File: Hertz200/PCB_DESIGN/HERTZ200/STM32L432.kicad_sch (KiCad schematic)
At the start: 10 parts

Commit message: schematics_Power_section
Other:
- moved on the sheet: C?
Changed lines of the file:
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@@
     (stroke (width 0) (type default) (color 0 0 0 0))
   )
-  (wire (pts (xy 96.52 71.12) (xy 96.52 73.66))
+  (wire (pts (xy 96.52 74.93) (xy 96.52 77.47))
     (stroke (width 0) (type default) (color 0 0 0 0))
   )
@@
     (stroke (width 0) (type default) (color 0 0 0 0))
   )
-  (wire (pts (xy 96.52 63.5) (xy 96.52 66.04))
+  (wire (pts (xy 96.52 63.5) (xy 96.52 69.85))
     (stroke (width 0) (type default) (color 0 0 0 0))
   )
@@
     (pin "1")
   )
-  (symbol (lib_id "power:GND") (at 96.52 73.66 0) (unit 1)
-    (in_bom yes) (on_board yes) (fields_autoplaced)
-    (property "Reference" "#PWR?" (id 0) (at 96.52 80.01 0)
-      (effects (font (size 1.27 1.27)) hide)
-    )
-    (property "Value" "GND" (id 1) (at 96.52 78.74 0))
-    (property "Footprint" "" (id 2) (at 96.52 73.66 0)
-      (effects (font (size 1.27 1.27)) hide)
-    )
-    (property "Datasheet" "" (id 3) (at 96.52 73.66 0)
+  (symbol (lib_id "power:GND") (at 96.52 77.47 0) (unit 1)
+    (in_bom yes) (on_board yes) (fields_autoplaced)
+    (property "Reference" "#PWR?" (id 0) (at 96.52 83.82 0)
+      (effects (font (size 1.27 1.27)) hide)
+    )
+    (property "Value" "GND" (id 1) (at 96.52 82.55 0))
+    (property "Footprint" "" (id 2) (at 96.52 77.47 0)
+      (effects (font (size 1.27 1.27)) hide)
+    )
+    (property "Datasheet" "" (id 3) (at 96.52 77.47 0)
       (effects (font (size 1.27 1.27)) hide)
     )
@@
     (pin "2")
   )
-  (symbol (lib_id "Device:C_Small") (at 96.52 68.58 0) (unit 1)
-    (in_bom yes) (on_board yes) (fields_autoplaced)
-    (property "Reference" "C?" (id 0) (at 99.06 67.3162 0)
-      (effects (font (size 1.27 1.27)) (justify left))
-    )
-    (property "Value" "0.1uF" (id 1) (at 99.06 69.8562 0)
-      (effects (font (size 1.27 1.27)) (justify left))
-    )
-    (property "Footprint" "" (id 2) (at 96.52 68.58 0)
-      (effects (font (size 1.27 1.27)) hide)
-    )
-    (property "Datasheet" "~" (id 3) (at 96.52 68.58 0)
-      (effects (font (size 1.27 1.27)) hide)
-    )
+  (symbol (lib_id "Device:C_Small") (at 96.52 72.39 0) (unit 1)
+    (in_bom yes) (on_board yes) (fields_autoplaced)
+    (property "Reference" "C?" (id 0) (at 99.06 71.1262 0)
+      (effects (font (size 1.27 1.27)) (justify left))
+    )
+    (property "Value" "0.1uF" (id 1) (at 99.06 73.6662 0)
+      (effects (font (size 1.27 1.27)) (justify left))
+    )
+    (property "Footprint" "" (id 2) (at 96.52 72.39 0)
+      (effects (font (size 1.27 1.27)) hide)
+    )
+    (property "Datasheet" "~" (id 3) (at 96.52 72.39 0)
+      (effects (font (size 1.27 1.27)) hide)
+    )

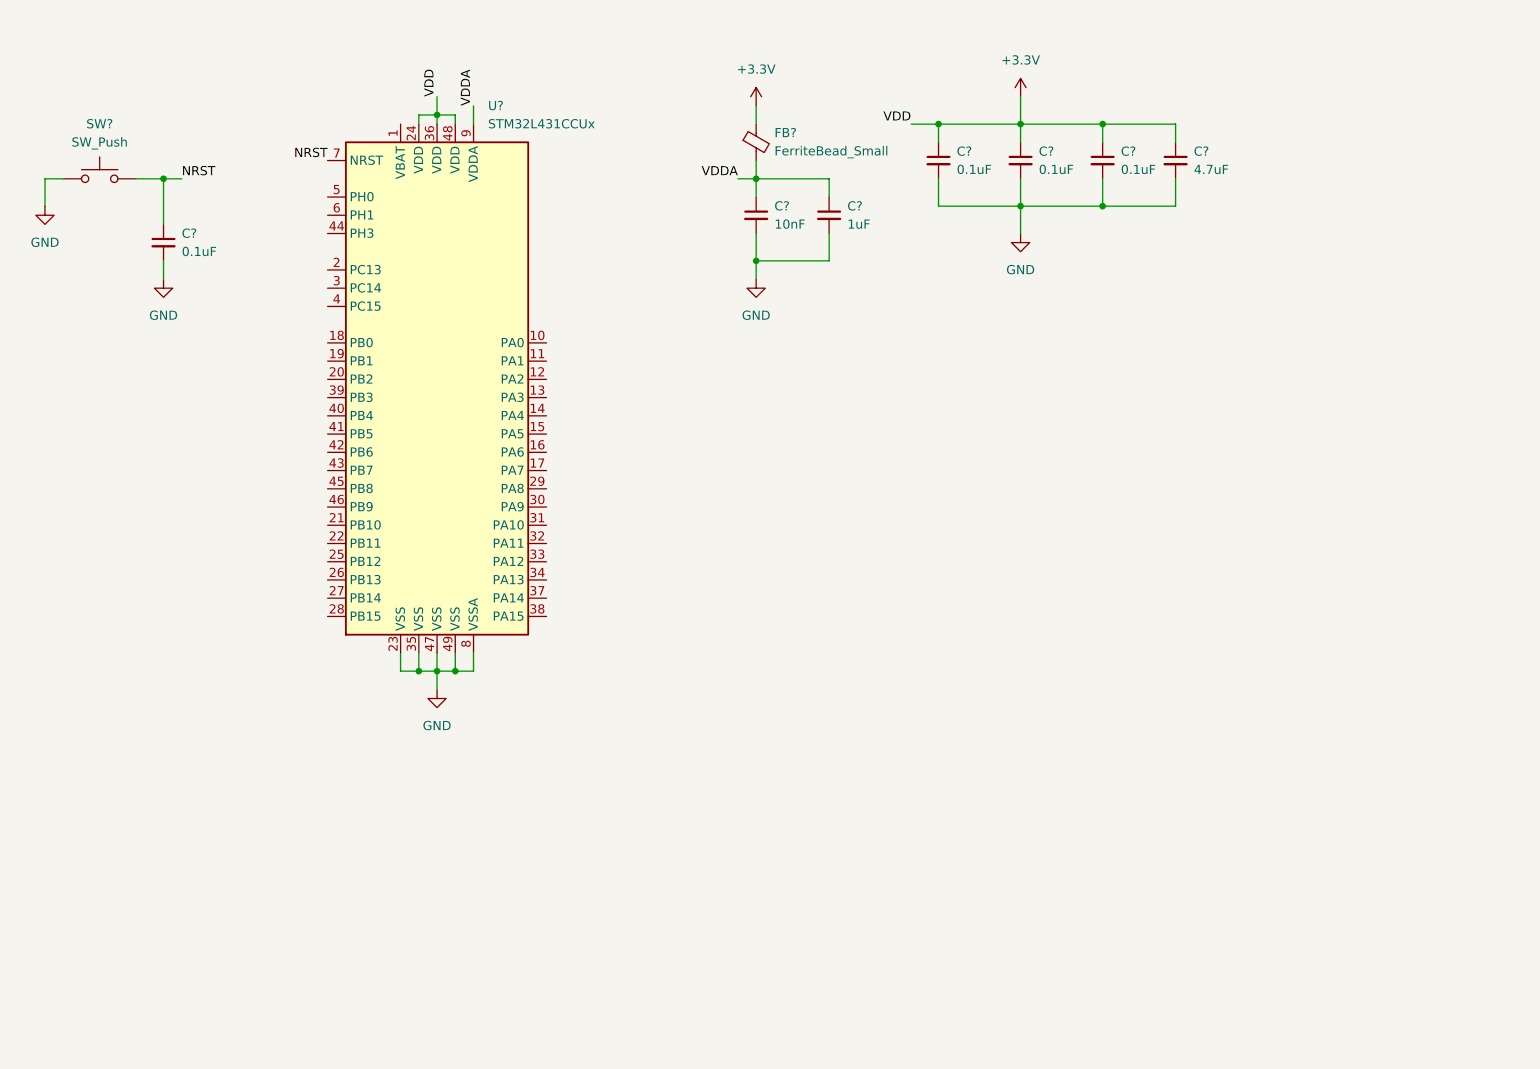
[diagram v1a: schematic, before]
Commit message: MCU-PIN-ASSIGNMENT
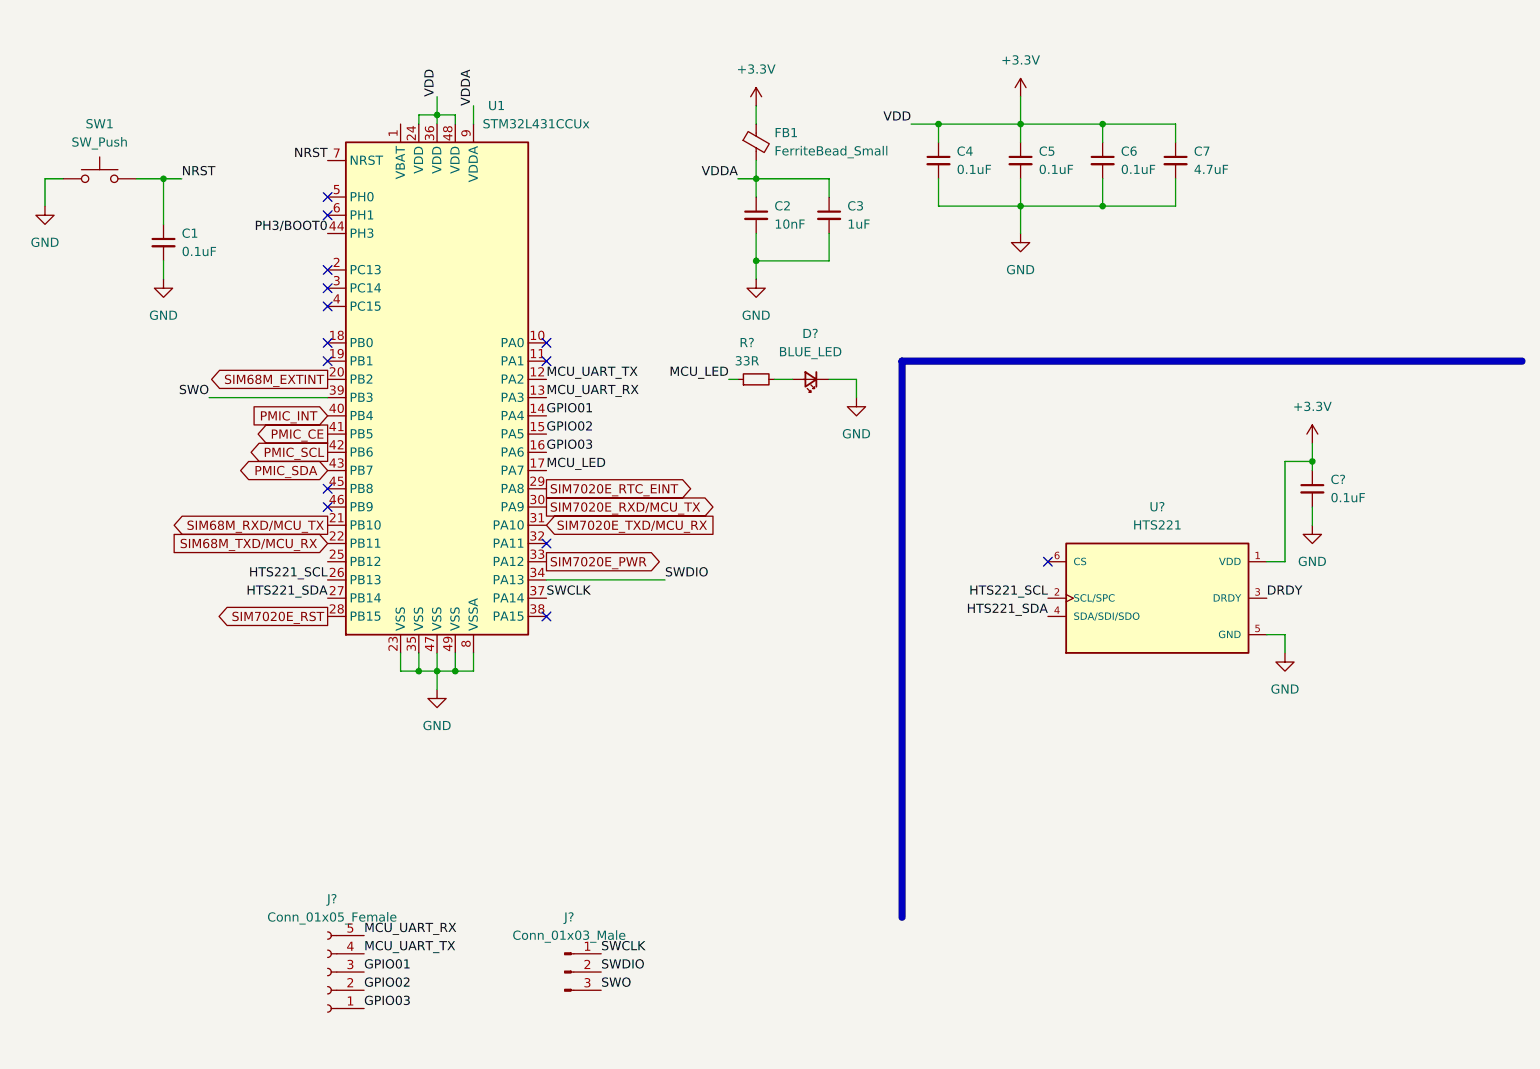
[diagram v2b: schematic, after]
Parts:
- added C?: 0.1uF, symbol Device:C_Small
- added D?: BLUE_LED, symbol Device:LED_Small
- added J?: Conn_01x03_Male, symbol Connector:Conn_01x03_Male
- added J?: Conn_01x05_Female, symbol Connector:Conn_01x05_Female
- added R?: 33R, symbol Device:R_Small
- added U?: HTS221, XDCR_HTS221, symbol HTS221:HTS221
- gave numbers to parts that had none: 10
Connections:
- net +3V3: now also C?.1, U?.1 (VDD)
- net GND: now also C?.2, D?.1 (K), U?.5 (GND)
- net MCU_UART_TX: now reaches U1.12 (PA2)
- net MCU_UART_TX: now also J?.4 (Pin_4)
- net MCU_UART_RX: now reaches U1.13 (PA3)
- net MCU_UART_RX: now also J?.5 (Pin_5)
- net GPIO01: now reaches U1.14 (PA4)
- net GPIO01: now also J?.3 (Pin_3)
- net GPIO02: now reaches U1.15 (PA5)
- net GPIO02: now also J?.2 (Pin_2)
- net GPIO03: now reaches U1.16 (PA6)
- net GPIO03: now also J?.1 (Pin_1)
- net MCU_LED: now reaches U1.17 (PA7)
- net MCU_LED: now also R?.1
- net SIM68M_EXTINT: now reaches U1.20 (PB2)
- net SIM68M_RXD/MCU_TX: now reaches U1.21 (PB10)
- net SIM68M_TXD/MCU_RX: now reaches U1.22 (PB11)
- net HTS221_SCL: now reaches U1.26 (PB13)
- net HTS221_SCL: now also U?.2 (SCL/SPC)
- net HTS221_SDA: now reaches U1.27 (PB14)
- net HTS221_SDA: now also U?.4 (SDA/SDI/SDO)
- net SIM7020E_RST: now reaches U1.28 (PB15)
- net SIM7020E_RTC_EINT: now reaches U1.29 (PA8)
- net SIM7020E_RXD/MCU_TX: now reaches U1.30 (PA9)
- net SIM7020E_TXD/MCU_RX: now reaches U1.31 (PA10)
- net SIM7020E_PWR: now reaches U1.33 (PA12)
- net SWDIO: now reaches U1.34 (PA13)
- net SWDIO: now also J?.2 (Pin_2)
- net SWCLK: now reaches U1.37 (PA14)
- net SWCLK: now also J?.1 (Pin_1)
- net SWO: now reaches U1.39 (PB3)
- net SWO: now also J?.3 (Pin_3)
- net PMIC_INT: now reaches U1.40 (PB4)
- net PMIC_CE: now reaches U1.41 (PB5)
- net PMIC_SCL: now reaches U1.42 (PB6)
- net PMIC_SDA: now reaches U1.43 (PB7)
- net PH3/BOOT0: now reaches U1.44 (PH3)
- new net: D?.2 (A), R?.2
- new net DRDY: U?.3 (DRDY)
- no-connect marks 0 -> 14

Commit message: schamtics_finish
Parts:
- removed J?: Conn_01x05_Female, symbol Connector:Conn_01x05_Female
- added J6: Conn_01x07_Male, symbol Connector:Conn_01x07_Male
- gave numbers to parts that had none: 5
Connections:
- net GPIO02: now also J6.4 (Pin_4)
- net GPIO03: now also J6.5 (Pin_5)
- net GPIO4: now reaches U1.18 (PB0)
- net GPIO5: now reaches U1.19 (PB1)
- net GPIO01 renamed SIM7020E_GPIO1
- net MCU_UART_RX renamed SIM7020E_UART2_TXD/u_RX
- net MCU_UART_TX renamed SIM7020E_UART2_RXD/u_TX
- new net GPIO04: J6.6 (Pin_6)
- new net GPIO05: J6.7 (Pin_7)
- no-connect marks 14 -> 17
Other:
- moved on the sheet: D5, R25

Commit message: Component_selection
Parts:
- C1, C2, C3, C38, C4, C5, C6, C7: footprint (none) -> Capacitor_SMD:C_0603_1608Metric
- D5: footprint (none) -> LED_SMD:LED_0805_2012Metric
- J6: footprint (none) -> Connector_PinHeader_2.54mm:PinHeader_1x07_P2.54mm_Vertical
- J7: footprint (none) -> Connector_PinHeader_2.54mm:PinHeader_1x03_P2.54mm_Vertical
- R25: footprint (none) -> Resistor_SMD:R_0603_1608Metric
- SW1: footprint (none) -> TS04-66-75-BK-160-SMT:SW_TS04-66-75-BK-160-SMT
- U6: footprint XDCR_HTS221 -> HTS221:XDCR_HTS221
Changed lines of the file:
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@@
     (property "Reference" "J7" (id 0) (at 153.035 166.37 0))
     (property "Value" "Conn_01x03_Male" (id 1) (at 153.035 168.91 0))
-    (property "Footprint" "" (id 2) (at 152.4 173.99 0)
+    (property "Footprint" "Connector_PinHeader_2.54mm:PinHeader_1x03_P2.54mm_Vertical" (id 2) (at 152.4 173.99 0)
       (effects (font (size 1.27 1.27)) hide)
     )
@@
     (property "Reference" "U6" (id 0) (at 234.95 109.22 0))
     (property "Value" "HTS221" (id 1) (at 234.95 111.76 0))
-    (property "Footprint" "XDCR_HTS221" (id 2) (at 234.95 121.92 0)
+    (property "Footprint" "HTS221:XDCR_HTS221" (id 2) (at 234.95 121.92 0)
       (effects (font (size 1.27 1.27)) (justify left bottom) hide)
     )
@@
       (effects (font (size 1.27 1.27)) (justify left))
     )
-    (property "Footprint" "" (id 2) (at 256.54 106.68 0)
+    (property "Footprint" "Capacitor_SMD:C_0603_1608Metric" (id 2) (at 256.54 106.68 0)
       (effects (font (size 1.27 1.27)) hide)
     )
@@
     (property "Reference" "R25" (id 0) (at 170.18 123.19 90))
     (property "Value" "33R" (id 1) (at 170.18 125.73 90))
-    (property "Footprint" "" (id 2) (at 171.45 128.27 0)
+    (property "Footprint" "Resistor_SMD:R_0603_1608Metric" (id 2) (at 171.45 128.27 0)
       (effects (font (size 1.27 1.27)) hide)
     )
@@
     (property "Reference" "SW1" (id 0) (at 87.63 55.88 0))
     (property "Value" "SW_Push" (id 1) (at 87.63 58.42 0))
-    (property "Footprint" "" (id 2) (at 87.63 58.42 0)
+    (property "Footprint" "TS04-66-75-BK-160-SMT:SW_TS04-66-75-BK-160-SMT" (id 2) (at 87.63 58.42 0)
       (effects (font (size 1.27 1.27)) hide)
     )
@@
       (effects (font (size 1.27 1.27)) (justify left))
     )
-    (property "Footprint" "" (id 2) (at 96.52 72.39 0)
+    (property "Footprint" "Capacitor_SMD:C_0603_1608Metric" (id 2) (at 96.52 72.39 0)
       (effects (font (size 1.27 1.27)) hide)
     )
@@
       (effects (font (size 1.27 1.27)) (justify left))
     )
-    (property "Footprint" "" (id 2) (at 189.23 68.58 0)
+    (property "Footprint" "Capacitor_SMD:C_0603_1608Metric" (id 2) (at 189.23 68.58 0)
       (effects (font (size 1.27 1.27)) hide)
     )
@@
     (property "Reference" "D5" (id 0) (at 179.0065 121.92 0))
     (property "Value" "BLUE_LED" (id 1) (at 179.0065 124.46 0))
-    (property "Footprint" "" (id 2) (at 179.07 128.27 90)
+    (property "Footprint" "LED_SMD:LED_0805_2012Metric" (id 2) (at 179.07 128.27 90)
       (effects (font (size 1.27 1.27)) hide)
     )
@@
     (property "Reference" "J6" (id 0) (at 120.015 163.83 0))
     (property "Value" "Conn_01x07_Male" (id 1) (at 120.015 166.37 0))
-    (property "Footprint" "" (id 2) (at 119.38 176.53 0)
+    (property "Footprint" "Connector_PinHeader_2.54mm:PinHeader_1x07_P2.54mm_Vertical" (id 2) (at 119.38 176.53 0)
       (effects (font (size 1.27 1.27)) hide)
     )
@@
       (effects (font (size 1.27 1.27)) (justify left))
     )
-    (property "Footprint" "" (id 2) (at 237.49 60.96 0)
+    (property "Footprint" "Capacitor_SMD:C_0603_1608Metric" (id 2) (at 237.49 60.96 0)
       (effects (font (size 1.27 1.27)) hide)
     )
@@
       (effects (font (size 1.27 1.27)) (justify left))
     )
-    (property "Footprint" "" (id 2) (at 215.9 60.96 0)
+    (property "Footprint" "Capacitor_SMD:C_0603_1608Metric" (id 2) (at 215.9 60.96 0)
       (effects (font (size 1.27 1.27)) hide)
     )
@@
       (effects (font (size 1.27 1.27)) (justify left))
     )
-    (property "Footprint" "" (id 2) (at 179.07 68.58 0)
+    (property "Footprint" "Capacitor_SMD:C_0603_1608Metric" (id 2) (at 179.07 68.58 0)
       (effects (font (size 1.27 1.27)) hide)
     )
@@
       (effects (font (size 1.27 1.27)) (justify left))
     )
-    (property "Footprint" "" (id 2) (at 227.33 60.96 0)
+    (property "Footprint" "Capacitor_SMD:C_0603_1608Metric" (id 2) (at 227.33 60.96 0)
       (effects (font (size 1.27 1.27)) hide)
     )
@@
       (effects (font (size 1.27 1.27)) (justify left))
     )
-    (property "Footprint" "" (id 2) (at 204.47 60.96 0)
-      (effects (font (size 1.27 1.27)) hide)
-    )
+    (property "Footprint" "Capacitor_SMD:C_0603_1608Metric" (id 2) (at 204.47 60.96 0)
+      (effects (font (size 1.27 1.27)) hide)
+    )
